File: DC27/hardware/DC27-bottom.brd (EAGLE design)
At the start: 102.4 x 117.6 mm, 2 parts

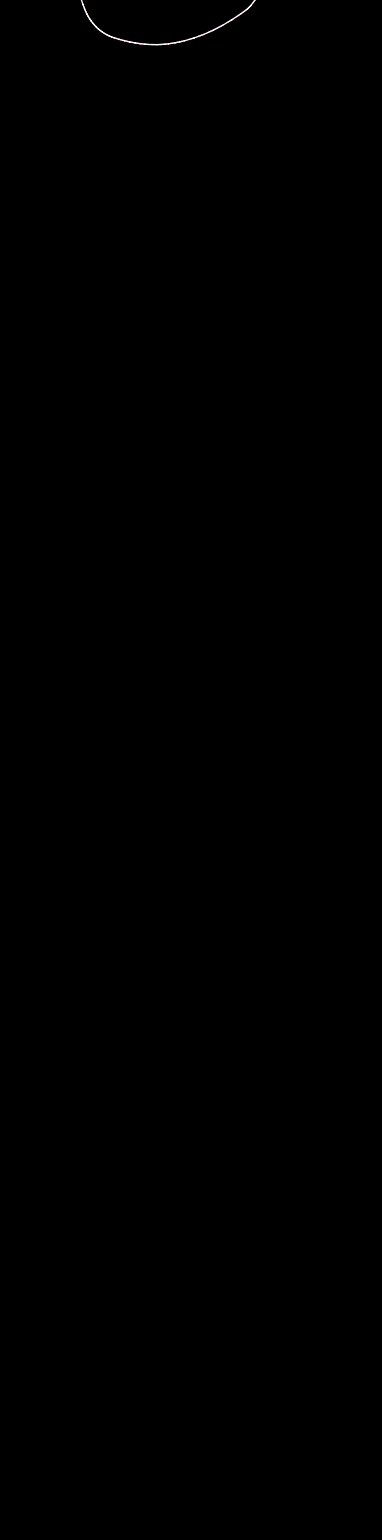
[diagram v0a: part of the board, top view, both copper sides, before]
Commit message: moving over schema
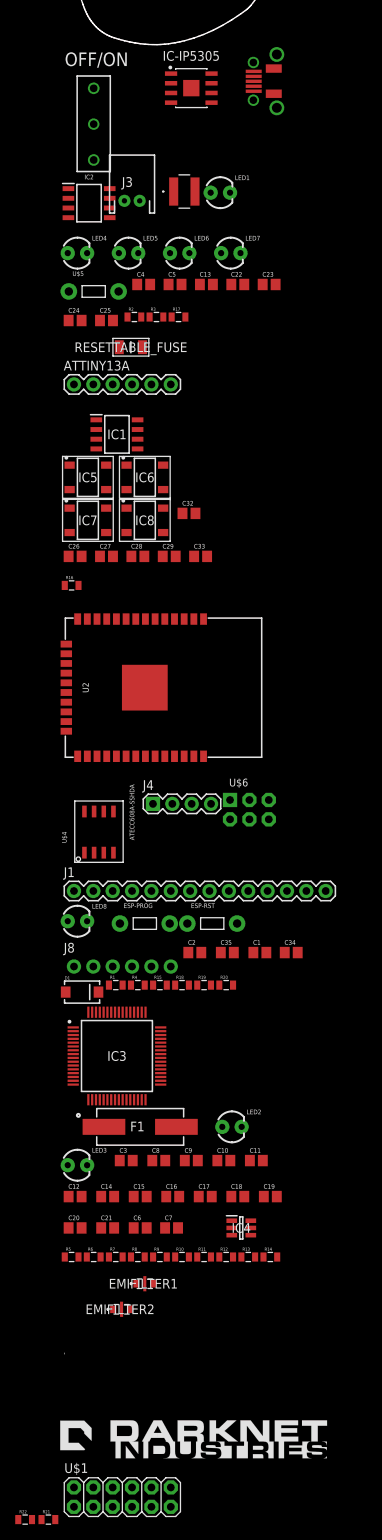
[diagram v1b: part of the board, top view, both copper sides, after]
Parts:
- removed U$2: CMD_C0DE_LOGO, darknet_parts_library:CMD_C0DE_LOGO
- added ATTINY13A: Header, connector:1X06
- added C1, C13, C22, C23, C24, C25: 10 uf, passives:C0805
- added C10, C11, C12, C14, C15, C16, C17, C19, C21, C3, C32, C35, C8: 0.1 uF, passives:C0805
- added C18, C2, C20: 4.7 uF, passives:C0805
- added C26, C27, C28, C29: 15 pF, passives:C0805
- added C33, C34: 10 uF, passives:C0805
- added C4, C5: 1 uF, passives:C0805
- added C6, C7: 27 pF, passives:C0805
- added C9: 3.3 uF, passives:C0805
- added D1: (no value), passives:SMA-DIODE
- added EMIFILTER1, EMIFILTER2: MEM2012S101RT, passives:MEM2012S101RT
- added ESP-PROG, ESP-RST: UserButton, dc-26:TACTILE-2PIN-NARROW
- added F1: ABLS-12.000MHZ-B4-T, crystals-timing:HC/49US-(AT49)_1
- added IC-IP5305: IP5305ESOP8, charging-ic:SOIC127P600X165-8
- added IC1: ATTINY13A-SSU, ICs:SOIC127P600X175-8N
- added IC2: LDL112D33R, voltage-regulator:SOIC127P600X175-8N
- added IC3: FT2232HL-REEL, ICs:QFP50P1200X1200X160-64N
- added IC4: 93LC46BT-I_OT, eeprom:SOT95P270X145-6N
- added IC5, IC6, IC7, IC8: APA104, leds:APA104
- added J1: (no value), connector:1X14
- added J3: (no value), connector:JST-2-PTH
- added J4: DN PAIR, connector:1X04
- added J8: (no value), connector:1X06_NO_SILK_YES_STOP
- added L1: 2.2uH, passives:IND_TAIYO_NRS4018
- added LED1, LED4, LED5, LED6, LED7, LED8: (no value), leds:LED3MM
- added LED2: rx-led, leds:LED3MM
- added LED3: tx-led, leds:LED3MM
- added OFF/ON: (no value), switches:SWITCH-SPDT
- added R1, R4: 10K, dc-26:0805
- added R10: 2.2K, passives:0805
- added R11, R12: 56, passives:0805
- added R13, R14: 100 R, passives:0805
- added R15, R18, R19, R20: 100 R, dc-26:0805
- added R16: 4.7 K, passives:0805
- added R17, R22: 10 K, passives:0805
- added R2: 10 R, passives:0805
- added R21: 4K7, passives:0805
- added R3: 20 R, passives:0805
- added R5: 1K, passives:0805
- added R6: 12 K, passives:0805
- added R7, R8, R9: 10K, passives:0805
- added RESETTABLE_FUSE: 0ZCJ0050FF2G, passives:FUSC3216X55N
- added U$3: DX4R005JJ2DX4R005JJ2, connector:DX4R005JJ2
- added U$4: ATECC608A-SSHDA, ICs:8-SOIC
- added U$5: SWITCH_TACTILETACTILE-2PIN-NARROW, switches:TACTILE-2PIN-NARROW
- added U$6: DC-27-SAO, defcon:3X2
- added U$7: KRUX_LOGO, logos:KRUX_LOGO
- added U$8: CMD_C0DE_LOGO, logos:CMD_C0DE_LOGO
- added U$9: DN_LOGODC26, logos:DN_LOGO_DC26
- added U2: ESP-WROOM-32, ICs:ESP-WROOM-32
- U$1: value KRUX_LOGO -> M06X2; device darknet_parts_library:KRUX_LOGO -> connector:2X6
- moved U$1 291.8 mm to (90.1, -107.6), flipped to the top
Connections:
- new net ATTINY_ESP_CON: ATTINY13A.2, IC1.2, R19.1
- new net DISPLAY_BACKLIT: C34.1, J1.4, R18.2
- new net DISPLAY_CS: J1.5, U2.28
- new net DISPLAY_DATA_CMD: J1.3, U2.26
- new net DISPLAY_RESET: C2.1, J1.2, R15.2
- new net DISPLAY_SD_MISO: J1.8, U2.31
- new net DISPLAY_SD_MOSI: J1.13, U2.37
- new net DISPLAY_SD_SCK: J1.7, U2.30
- new net EECLK: IC3.62, IC4.4, R8.2
- new net EECS: IC3.63, IC4.5, R7.1
- new net EEDATA: IC3.61, IC4.3, R10.2
- new net ESP-EN: ESP-RST.P$2, R4.1, U2.3
- new net ESP-IO0: ESP-PROG.P$1, R1.1, U2.25
- new net ESP_ATTINY_CON: R19.2, U2.24
- new net ESP_LED1: R20.2, U2.27
- new net GND: C1.2, C10.2, C11.2, C12.2, C13.1, C14.2, C15.2, C16.2, C17.2, C18.2, C19.2, C2.2, C20.2, C21.2, C22.1, C23.1, C24.1, C25.2, C26.2, C27.2, C28.2, C29.2, C3.2, C32.2, C33.2, C34.2, C35.2, C4.2, C5.2, C6.2, C7.2, C8.2, C9.2, EMIFILTER1.2, EMIFILTER1.4, EMIFILTER2.2, EMIFILTER2.4, ESP-PROG.P$2, ESP-RST.P$1, IC-IP5305.GND, IC1.4, IC2.2, IC2.3, IC2.6, IC2.7, IC3.1, IC3.10, IC3.11, IC3.13, IC3.15, IC3.25, IC3.35, IC3.47, IC3.5, IC3.51, IC4.2, IC5.3, IC6.3, IC7.3, IC8.3, J1.14, J3.2, J8.3, LED7.K, LED8.K, OFF/ON.1, R22.1, R6.2, U$1.2, U$3.GND, U$3.P$10, U$3.P$11, U$3.P$6, U$3.P$7, U$3.P$8, U$3.P$9, U$4.GND, U$5.P$1, U$6.4, U2.1, U2.15, U2.38, U2.GND
- new net GPIO_APA104_DATA: ATTINY13A.1, IC1.3, IC5.4
- new net JTAG_CLK: IC3.16, U2.16
- new net JTAG_TDI: IC3.17, U2.14
- new net JTAG_TDO: IC3.18, U2.23
- new net JTAG_TMS: IC3.19, U2.13
- new net N$1: D1.C, U$6.1
- new net N$10: C23.2, C24.2, IC-IP5305.VOUT, RESETTABLE_FUSE.1
- new net N$11: LED2.A, R11.1
- new net N$12: IC6.2, IC7.4
- new net N$13: LED3.A, R12.1
- new net N$14: IC-IP5305.LED2, LED5.A, LED6.K
- new net N$15: IC-IP5305.LED3, LED1.K, LED4.A, LED5.K, LED6.A
- new net N$16: C22.2, R2.2
- new net N$17: IC-IP5305.SW, L1.2
- new net N$18: C18.1, C19.1, EMIFILTER2.3, IC3.9
- new net N$19: C20.1, C21.1, EMIFILTER1.3, IC3.4
- new net N$2: IC2.5, OFF/ON.2
- new net N$20: C25.1, IC-IP5305.BAT, J3.1, L1.1
- new net N$21: IC-IP5305.KEY, R17.1, R3.1
- new net N$22: IC7.2, IC8.4
- new net N$24: LED7.A, R3.2
- new net N$25: R17.2, U$5.P$2
- new net N$31: R14.1, U$1.9
- new net N$32: R13.1, U$1.7
- new net N$4: IC5.2, IC6.4
- new net N$5: IC-IP5305.LED1, LED1.A, LED4.K
- new net N$6: IC3.14, R5.2
- new net N$7: IC3.6, R6.1
- new net N$8: IC4.1, R10.1, R9.1
- new net N$9: LED8.A, R20.1
- new net OSCI: C6.1, F1.2, IC3.2
- new net OSCO: C7.1, F1.1, IC3.3
- new net PAIR_RX: J4.2, U2.6
- new net PAIR_TX: J4.1, U2.10
- new net PB0: ATTINY13A.6, IC1.5
- new net PB1: ATTINY13A.5, IC1.6
- new net PB2: ATTINY13A.4, IC1.7
- new net PB5: ATTINY13A.3, IC1.1, R16.1
- new net PROG_RX: R14.2, U2.34
- new net PROG_TX: R13.2, U2.35
- new net PWREN: IC3.60, U$1.1
- new net PWRSAV: IC3.59, R21.2, R22.2
- new net RXD_LED: IC3.54, LED2.K
- new net RXD_SPI_PROM_MOSI: IC3.39, J1.11, U$1.8
- new net SAO-GPIO1: U$6.3
- new net SAO-GPIO2: U$6.6
- new net SCL: J1.12, U$4.SCL, U$6.5, U2.36
- new net SDA: J1.9, U$4.SDA, U$6.2, U2.33
- new net SD_CS: J1.6, U2.29
- new net SPI_PROM_CS: IC3.41, U$1.4
- new net SPI_PROM_MISO: IC3.40, U$1.6
- new net SUSPEND: IC3.36, U$1.3
- new net SVN: J4.3, U2.5
- new net SVP: J4.4, U2.4
- new net TOUCH_CLK: J8.2, U2.11
- new net TOUCH_CS: J8.1, U2.12
- new net TOUCH_DATA_IN: J8.6, U2.7
- new net TOUCH_DATA_OUT: J8.4, U2.9
- new net TOUCH_IRQ: J8.5, U2.8
- new net TXD_LED: IC3.55, LED3.K
- new net TXD_SPI_PROM_CLK: IC3.38, J1.10, U$1.10
- new net USB_DM: IC3.7, U$3.D-
- new net USB_DP: IC3.8, U$3.D+
- new net VBAT: C26.1, C27.1, C28.1, C29.1, C32.1, C33.1, C4.1, IC1.8, IC2.4, IC5.1, IC6.1, IC7.1, IC8.1, OFF/ON.3, R16.2, RESETTABLE_FUSE.2
- new net VCC: C1.1, C11.1, C14.1, C15.1, C16.1, C3.1, C35.1, C5.1, C8.1, D1.A, EMIFILTER1.1, EMIFILTER2.1, IC2.1, IC3.20, IC3.31, IC3.42, IC3.50, IC3.56, IC4.6, J1.1, R1.2, R11.2, R12.2, R15.1, R18.1, R4.2, R5.1, R7.2, R8.1, R9.2, U$1.12, U$4.VCC, U2.2
- new net VCC1.8: C10.1, C12.1, C17.1, C9.1, IC3.12, IC3.37, IC3.49, IC3.64
- new net VCC5V: C13.2, IC-IP5305.VIN, R2.1, R21.1, U$3.+5V

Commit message: dc27 board started for darknet 8
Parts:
- removed ATTINY13A: Header, connector:1X06
- removed C32: 0.1 uF, passives:C0805
- removed C33: 10 uF, passives:C0805
- removed F1: ABLS-12.000MHZ-B4-T, crystals-timing:HC/49US-(AT49)_1
- removed IC1: ATTINY13A-SSU, ICs:SOIC127P600X175-8N
- removed IC5, IC6, IC7, IC8: APA104, leds:APA104
- removed J4: DN PAIR, connector:1X04
- removed J8: (no value), connector:1X06_NO_SILK_YES_STOP
- removed R19, R20: 100 R, dc-26:0805
- removed R21: 4K7, passives:0805
- added J2: JTAG, connector:2X4
- added R23, R24, R25, R26: 100 R, dc-26:0805
- added U$10: 2.4-SPI-TFT-TOUCH-SSD-MODULE, displays:2.4-SPI-TFT-TOUCH-SSD-MODULE
- added U$11, U$12, U$13, U$14: APA1025050, leds:APA102_5050
- added U$2: XBP15SRV05W-G, passives:SOT-26P-XBP15SRV05W-G
- added Y1: ABM7-12.000MHZ-D2Y-T, crystals-timing:ABM7
- C1, C13, C22, C23, C24, C25: value 10 uf -> 10 uF
- C6, C7: value 27 pF -> 18 pF
- D1: value (none) -> SAO-Diode
- J1: value (none) -> DN PAIR; device connector:1X14 -> connector:2X3
- J3: value (none) -> Battery
- LED1: value (none) -> cl1
- LED4: value (none) -> cl2
- LED5: value (none) -> cl3
- LED6: value (none) -> cl4
- LED7: value (none) -> KeyLed
- LED8: value (none) -> ESP-LED
- OFF/ON: value (none) -> Brd Power; device switches:SWITCH-SPDT -> switches:SWITCH-SPDT_KIT
- R1, R4, R7, R8, R9: value 10K -> 10 K
- R10: value 2.2K -> 2.2 K
- R11, R12: value 56 -> 56 R
- R3: value 20 R -> 10 R
- R5: value 1K -> 1 K
- moved R22 169.6 mm to (32.0, 52.3)
- moved U$9 166.8 mm to (51.2, 58.8), flipped to the bottom
- moved R4 164.4 mm to (35.7, 112.8)
- moved C1 161.2 mm to (37.2, 106.5), turned to 270 degrees
- moved U$1 160.3 mm to (97.5, 52.6), turned to 90 degrees
- moved ESP-RST 160.3 mm to (31.1, 109.4), turned to 270 degrees
- moved R11 156.2 mm to (20.3, 55.0), turned to 270 degrees
- moved J1 151.2 mm to (7.62, 100.0), turned to 270 degrees
- moved R12 148.4 mm to (23.5, 45.7), turned to 90 degrees
- moved R14 146.7 mm to (96.0, 70.6), flipped to the bottom
- moved LED2 142.8 mm to (25.0, 56.4)
- moved D1 142.5 mm to (90.5, 102.4)
- moved R15 135.1 mm to (8.53, 59.0), turned to 180 degrees
- moved C6 132.0 mm to (41.6, 48.0), turned to 90 degrees
- moved C34 131.9 mm to (11.4, 42.1), turned to 270 degrees
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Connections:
- removed net ATTINY_ESP_CON: ATTINY13A.2, IC1.2, R19.1
- removed net ESP_ATTINY_CON: R19.2, U2.24
- removed net ESP_LED1: R20.2, U2.27
- removed net GPIO_APA104_DATA: ATTINY13A.1, IC1.3, IC5.4
- removed net JTAG_TDO: IC3.18, U2.23
- removed net N$12: IC6.2, IC7.4
- removed net N$22: IC7.2, IC8.4
- removed net N$4: IC5.2, IC6.4
- removed net N$9: LED8.A, R20.1
- removed net PB0: ATTINY13A.6, IC1.5
- removed net PB1: ATTINY13A.5, IC1.6
- removed net PB2: ATTINY13A.4, IC1.7
- removed net PB5: ATTINY13A.3, IC1.1, R16.1
- new net APA102_CLK: U$13.5, U2.24
- new net APA102_DATA: U$13.4, U2.27
- new net ESP_JTAG_CLK: J2.8, R23.1
- new net ESP_JTAG_TDI: J2.6, R25.1
- new net ESP_JTAG_TDO_LED: J2.4, LED8.A, R24.1
- new net ESP_JTAG_TMS: J2.2, R26.1
- new net FT_JTAG_CLK: IC3.16, J2.7
- new net FT_JTAG_TDI: IC3.17, J2.5
- new net FT_JTAG_TDO: IC3.18, J2.3
- new net FT_JTAG_TMS: IC3.19, J2.1
- new net JTAG_TDO_LED1: R24.2, U2.23
- new net N$28: U$11.6, U$12.6, U$13.6, U$14.6
- new net N$34: U$11.5, U$12.2
- new net N$35: U$11.4, U$12.3
- new net N$36: U$12.5, U$14.2
- new net N$37: U$12.4, U$14.3
- new net N$38: U$13.3, U$14.4
- new net N$39: U$13.2, U$14.5
- net DISPLAY_BACKLIT: now also U$10.8; no longer J1.4
- net DISPLAY_CS: now also U$10.3; no longer J1.5
- net DISPLAY_DATA_CMD: now also U$10.5; no longer J1.3
- net DISPLAY_RESET: now also U$10.4; no longer J1.2
- net DISPLAY_SD_MISO: now also U$10.17, U$10.9; no longer J1.8
- net DISPLAY_SD_MOSI: now also U$10.16, U$10.6; no longer J1.13
- net DISPLAY_SD_SCK: now also U$10.18, U$10.7; no longer J1.7
- net ESP-IO0: now also ESP-PROG.P$2; no longer ESP-PROG.P$1
- net GND: now also ESP-PROG.P$1, U$10.2, U$2.P2; no longer C32.2, C33.2, ESP-PROG.P$2, IC1.4, IC5.3, IC6.3, IC7.3, IC8.3, J1.14, J8.3
- net JTAG_CLK: now also R23.2; no longer IC3.16
- net JTAG_TDI: now also R25.2; no longer IC3.17
- net JTAG_TMS: now also R26.2; no longer IC3.19
- net OSCI: now also Y1.2; no longer F1.2
- net OSCO: now also Y1.1; no longer F1.1
- net PAIR_RX: now also J1.3; no longer J4.2
- net PAIR_TX: now also J1.5; no longer J4.1
- net PWRSAV: now also R16.2; no longer R21.2
- net RXD_SPI_PROM_MOSI: no longer J1.11
- net SAO-GPIO1: now also J1.4
- net SAO-GPIO2: now also J1.6
- net SCL: no longer J1.12
- net SDA: no longer J1.9
- net SD_CS: now also U$10.15; no longer J1.6
- net SVN: now also J1.1; no longer J4.3
- net SVP: now also J1.2; no longer J4.4
- net TOUCH_CLK: now also U$10.10; no longer J8.2
- net TOUCH_CS: now also U$10.11; no longer J8.1
- net TOUCH_DATA_IN: now also U$10.12; no longer J8.6
- net TOUCH_DATA_OUT: now also U$10.13; no longer J8.4
- net TOUCH_IRQ: now also U$10.14; no longer J8.5
- net TXD_SPI_PROM_CLK: no longer J1.10
- net USB_DM: now also U$2.P1
- net USB_DP: now also U$2.P6
- net VBAT: no longer C26.1, C27.1, C28.1, C29.1, C32.1, C33.1, IC1.8, IC5.1, IC6.1, IC7.1, IC8.1, R16.2
- net VCC: now also C26.1, C27.1, C28.1, C29.1, U$10.1, U$11.1, U$12.1, U$13.1, U$14.1; no longer J1.1
- net VCC5V: now also R16.1; no longer R21.1
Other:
- board size 102.4 x 117.6 mm -> 102.4 x 201.9 mm

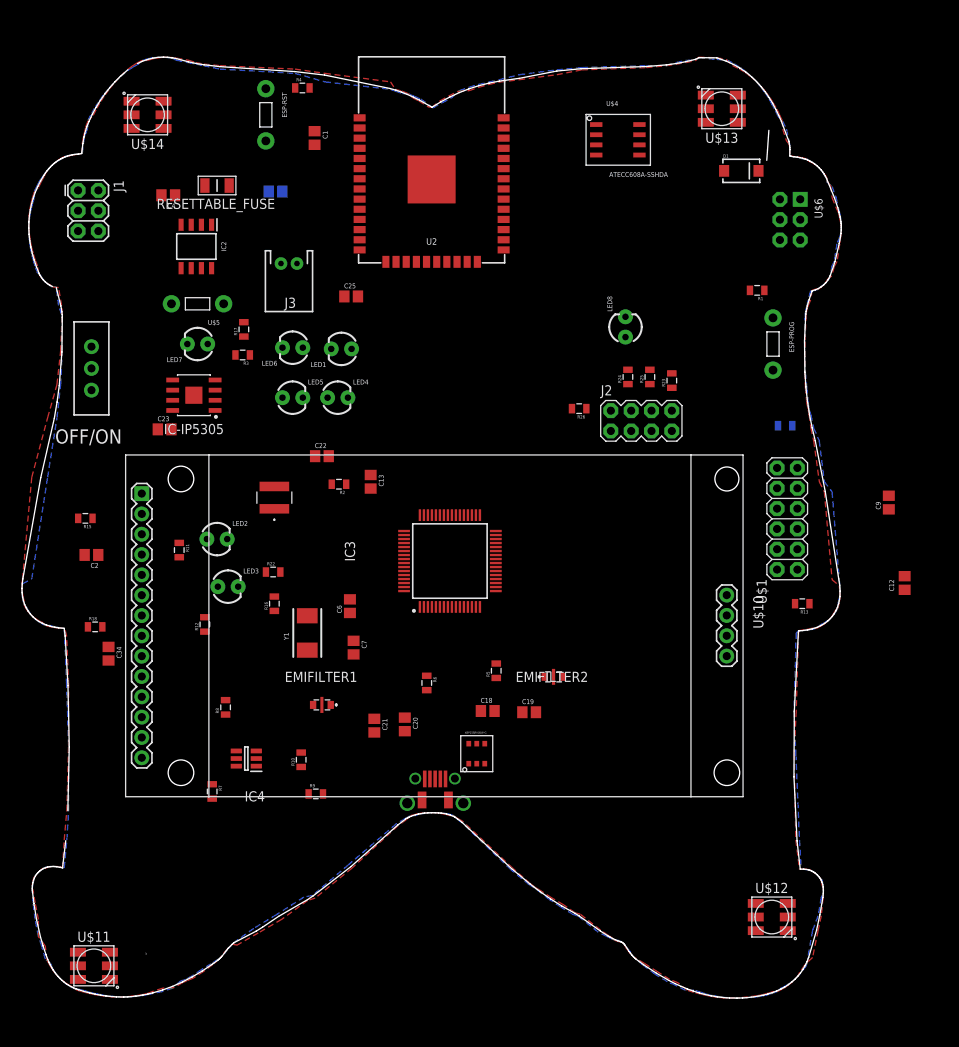
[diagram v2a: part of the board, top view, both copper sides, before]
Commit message: adding basic layout dc27 badge
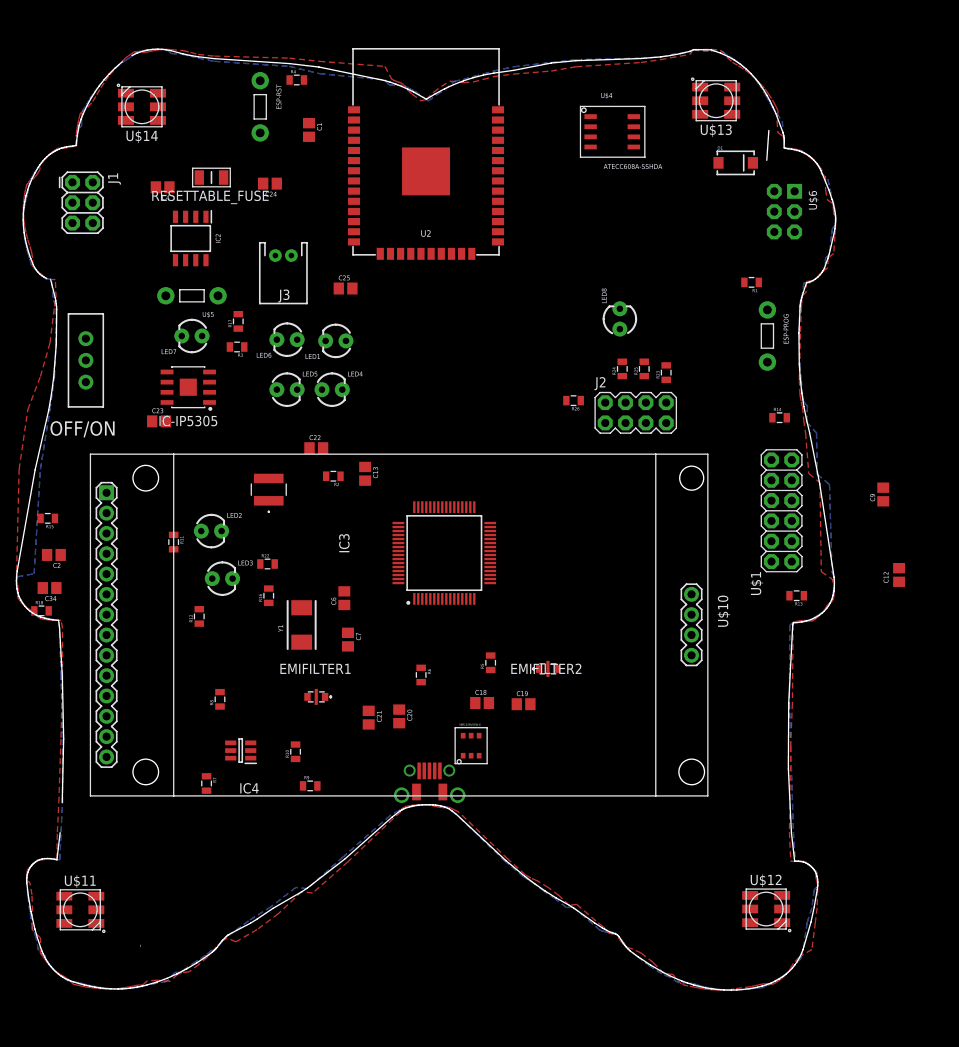
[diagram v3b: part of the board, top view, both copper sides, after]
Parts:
- moved C34 11.0 mm to (4.06, 50.3), turned to 180 degrees
- moved U$11 7.20 mm to (7.90, 10.0)
- moved R18 6.99 mm to (3.05, 47.4)
- moved C2 4.70 mm to (4.60, 54.4)
- moved R15 4.70 mm to (3.83, 59.0)
- moved U$10 4.40 mm to (9.16, 67.0)
- moved C1 1.22 mm to (36.5, 107.5)
- moved C18 1.22 mm to (58.1, 35.9)
- moved C20 1.22 mm to (47.8, 34.2)
- moved C22 1.22 mm to (37.4, 67.8)
- moved C6 1.22 mm to (40.9, 49.0)
- moved D1 1.22 mm to (89.8, 103.4)
- moved EMIFILTER1 1.22 mm to (37.4, 36.7)
- moved EMIFILTER2 1.22 mm to (66.4, 40.2)
- moved ESP-PROG 1.22 mm to (93.8, 81.8)
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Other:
- board size 102.4 x 201.9 mm -> 102.8 x 200.9 mm

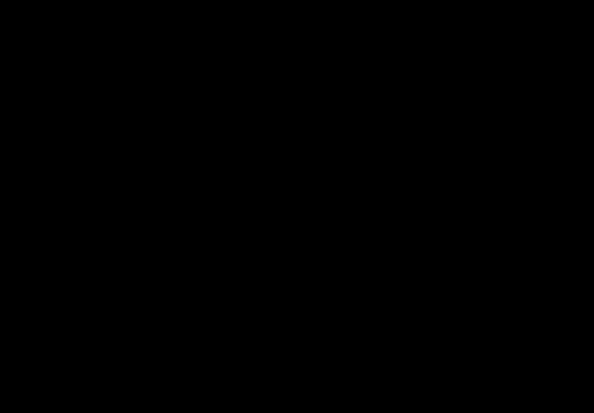
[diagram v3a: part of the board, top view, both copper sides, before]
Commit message: started on changes to not charlie plex the leds
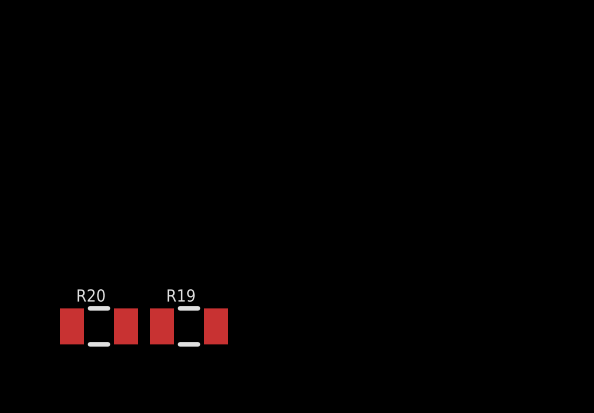
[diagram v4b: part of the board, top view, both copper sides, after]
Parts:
- added R19, R20: 4.7 K, dc-26:0805
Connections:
- net SCL: now also R20.1
- net SDA: now also R19.2
- net VCC: now also R19.1, R20.2

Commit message: basic layout nearly done
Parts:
- removed C26, C27, C28, C29: 15 pF, passives:C0805
- removed D1: SAO-Diode, passives:SMA-DIODE
- removed U$11, U$12, U$13, U$14: APA1025050, leds:APA102_5050
- removed U$6: DC-27-SAO, defcon:3X2
- added TOP-BOT-CONNECTOR: M06X2, connector:2X6
- LED1, LED2, LED3, LED4, LED5, LED6, LED7, LED8: device leds:LED3MM -> leds:LED-1206
- moved R20 164.6 mm to (65.0, 108.0), turned to 90 degrees
- moved R19 159.7 mm to (65.0, 104.0), turned to 270 degrees
- moved C17 156.4 mm to (55.2, 71.8), turned to 90 degrees
- moved C10 155.5 mm to (43.3, 58.9), turned to 180 degrees
- moved C16 132.2 mm to (51.9, 71.6), turned to 90 degrees
- moved C3 130.4 mm to (24.1, 53.8), turned to 180 degrees
- moved C8 127.5 mm to (42.6, 66.2), turned to 180 degrees
- moved C14 115.7 mm to (61.8, 65.9)
- moved C15 115.2 mm to (66.7, 57.5)
- moved C11 103.2 mm to (43.4, 63.0), turned to 180 degrees
- moved C4 95.5 mm to (70.1, 20.2), turned to 90 degrees
- moved OFF/ON 95.3 mm to (75.3, 10.6), turned to 231.9 degrees
- moved RESETTABLE_FUSE 92.0 mm to (65.4, 19.3), turned to 358.9 degrees
- moved IC2 91.2 mm to (76.0, 20.7), turned to 0 degrees
- moved C35 90.2 mm to (75.9, 106.5)
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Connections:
- removed net N$1: D1.C, U$6.1
- removed net N$28: U$11.6, U$12.6, U$13.6, U$14.6
- removed net N$34: U$11.5, U$12.2
- removed net N$35: U$11.4, U$12.3
- removed net N$36: U$12.5, U$14.2
- removed net N$37: U$12.4, U$14.3
- removed net N$38: U$13.3, U$14.4
- removed net N$39: U$13.2, U$14.5
- net APA102_CLK: now also TOP-BOT-CONNECTOR.5; no longer U$13.5
- net APA102_DATA: now also TOP-BOT-CONNECTOR.3; no longer U$13.4
- net GND: now also J3.1, LED7.C, LED8.C, TOP-BOT-CONNECTOR.11, TOP-BOT-CONNECTOR.12; no longer C26.2, C27.2, C28.2, C29.2, J3.2, LED7.K, LED8.K, U$6.4
- net N$14: now also LED6.C; no longer LED6.K
- net N$15: now also LED1.C, LED5.C; no longer LED1.K, LED5.K
- net N$20: now also J3.2; no longer J3.1
- net N$5: now also LED4.C; no longer LED4.K
- net RXD_LED: now also LED2.C; no longer LED2.K
- net SAO-GPIO1: now also TOP-BOT-CONNECTOR.8; no longer U$6.3
- net SAO-GPIO2: now also TOP-BOT-CONNECTOR.10; no longer U$6.6
- net SCL: now also TOP-BOT-CONNECTOR.4; no longer U$6.5
- net SDA: now also TOP-BOT-CONNECTOR.6; no longer U$6.2
- net TXD_LED: now also LED3.C; no longer LED3.K
- net VBAT: now also TOP-BOT-CONNECTOR.1
- net VCC: now also TOP-BOT-CONNECTOR.2; no longer C26.1, C27.1, C28.1, C29.1, D1.A, U$11.1, U$12.1, U$13.1, U$14.1
